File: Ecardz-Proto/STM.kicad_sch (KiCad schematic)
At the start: 0 parts

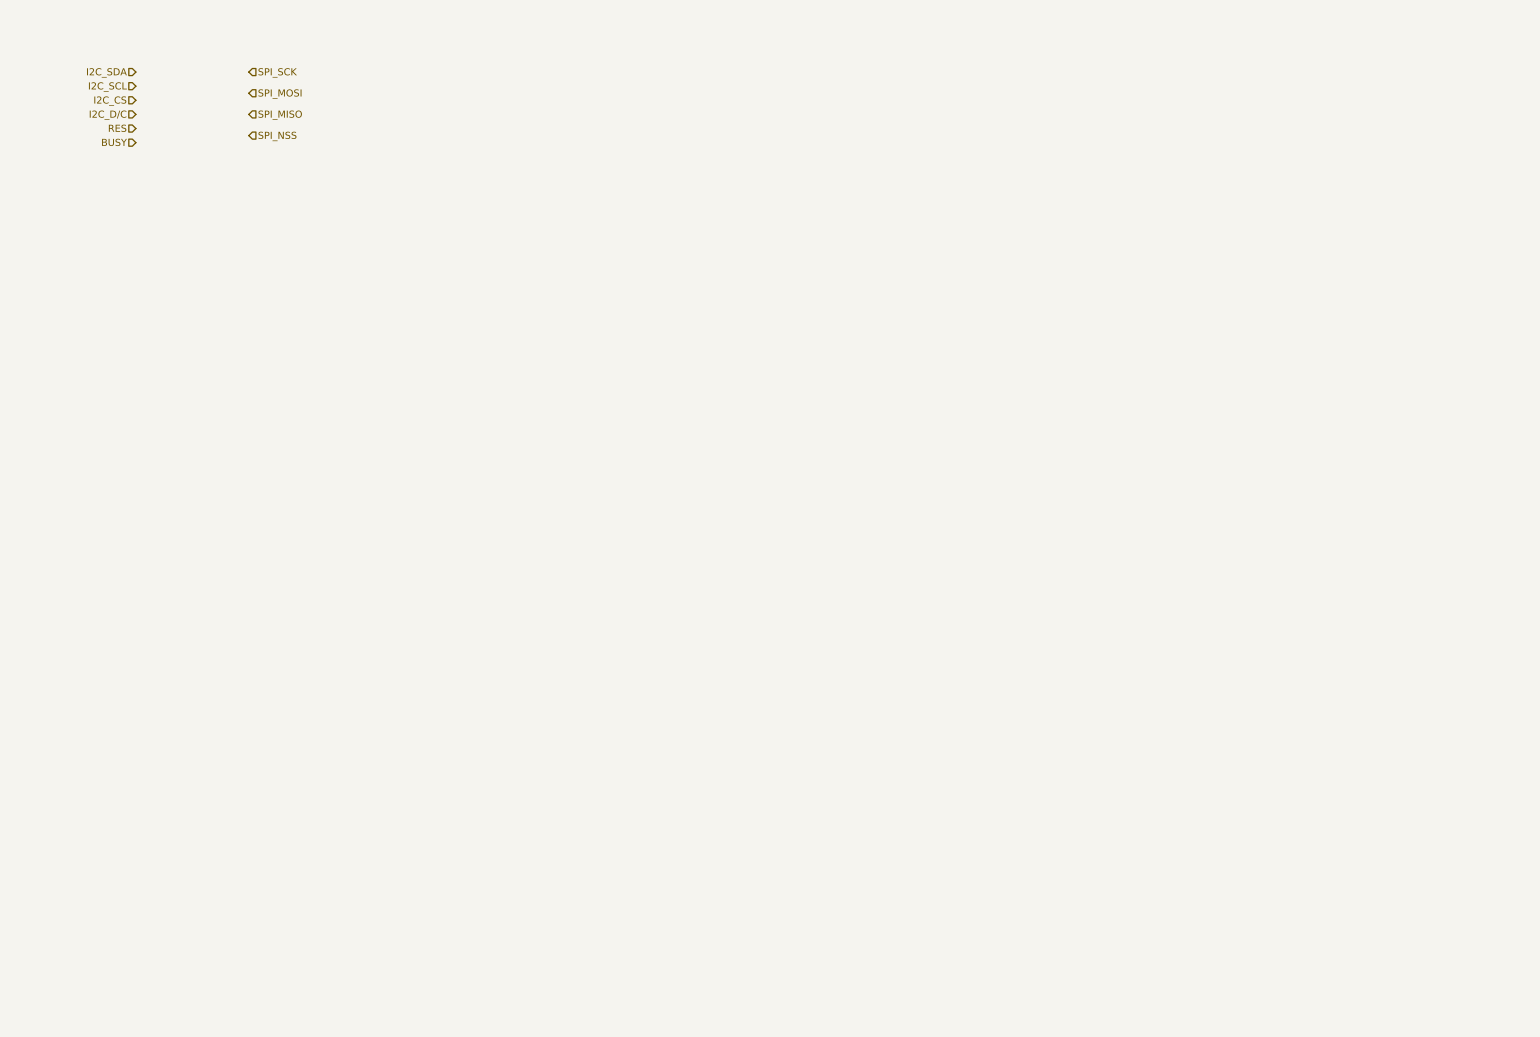
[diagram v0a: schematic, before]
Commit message: added STM and rpi pin connections.
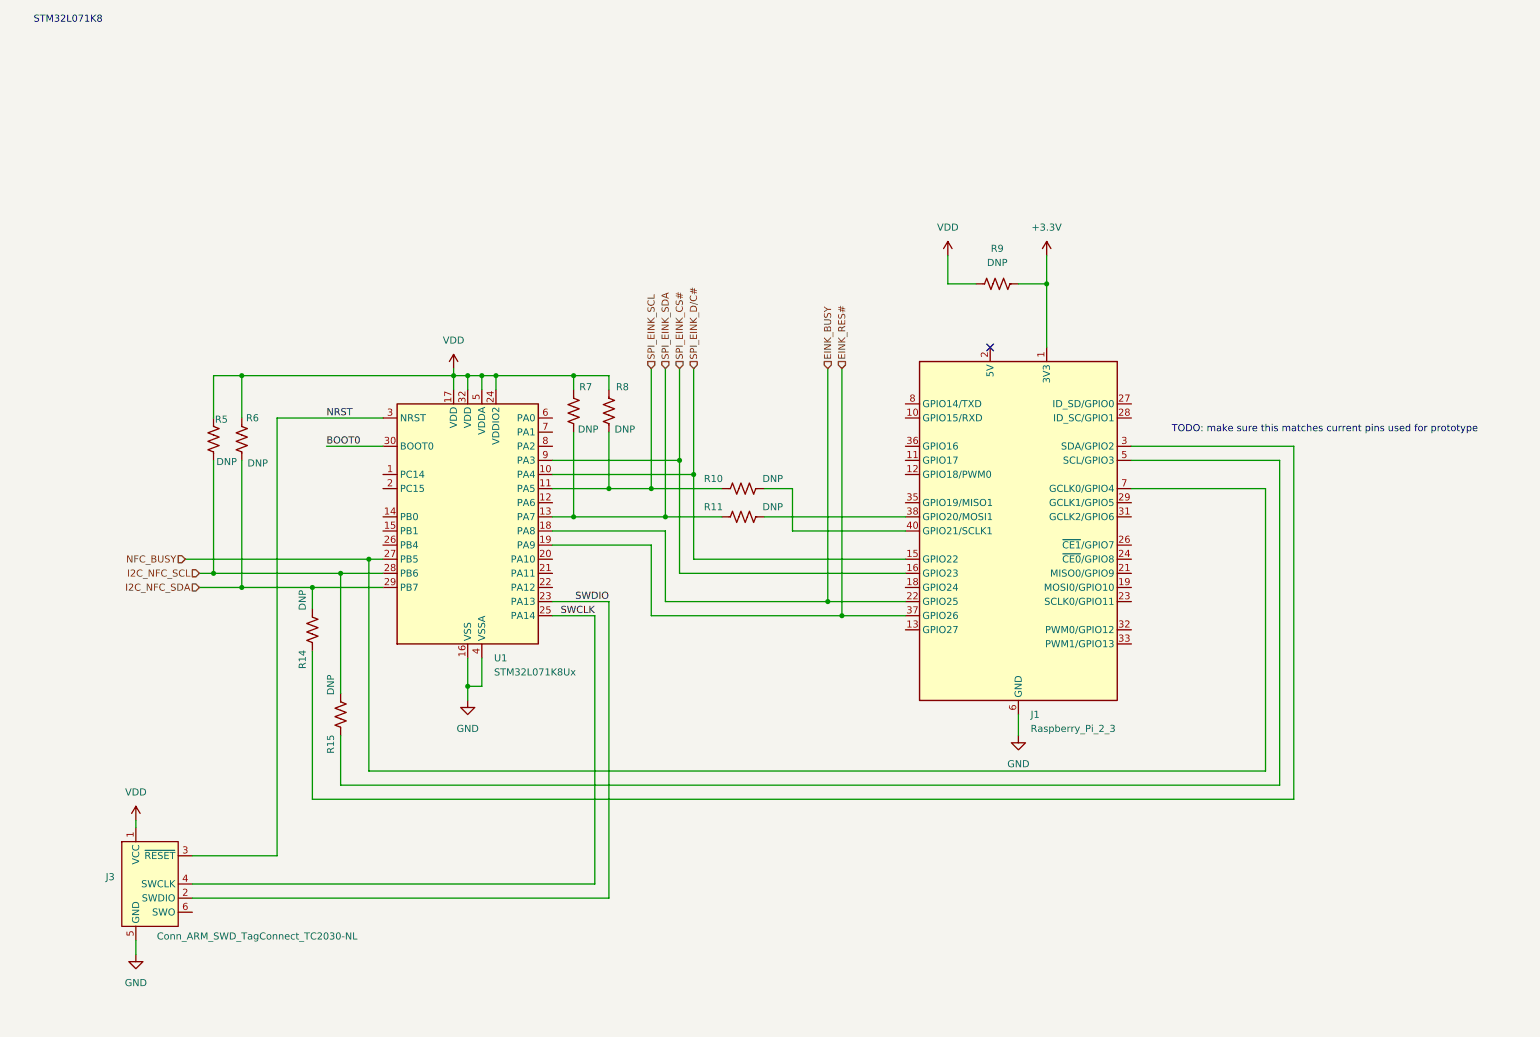
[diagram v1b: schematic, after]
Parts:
- added J1: Raspberry_Pi_2_3, symbol Connector:Raspberry_Pi_2_3
- added J3: Conn_ARM_SWD_TagConnect_TC2030-NL, Connector:Tag-Connect_TC2030-IDC-NL_2x03_P1.27mm_Vertical, symbol Connector:Conn_ARM_SWD_TagConnect_TC2030-NL
- added R10, R11, R14, R15, R5, R6, R7, R8, R9: DNP, Resistor_SMD:R_0603_1608Metric_Pad0.98x0.95mm_HandSolder, symbol Device:R_US
- added U1: STM32L071K8Ux, Package_DFN_QFN:QFN-32-1EP_5x5mm_P0.5mm_EP3.45x3.45mm, symbol MCU_ST_STM32L0:STM32L071K8Ux
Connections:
- new net: J1.5 (SCL/GPIO3), R15.1
- new net: J1.38 (GPIO20/MOSI1), R11.2
- new net: J1.2 (5V), J1.4 (5V)
- new net: J1.3 (SDA/GPIO2), R14.1
- new net: J1.40 (GPIO21/SCLK1), R10.2
- new net +3.3V: J1.1 (3V3), J1.17 (3V3), R9.2
- new net BOOT0: U1.30 (BOOT0)
- new net EINK_BUSY: J1.22 (GPIO25), U1.18 (PA8)
- new net EINK_RES#: J1.37 (GPIO26), U1.19 (PA9)
- new net GND: J1.14 (GND), J1.20 (GND), J1.25 (GND), J1.30 (GND), J1.34 (GND), J1.39 (GND), J1.6 (GND), J1.9 (GND), J3.5 (GND), U1.16 (VSS), U1.31 (VSS), U1.33 (VSS), U1.4 (VSSA)
- new net I2C_NFC_SCL: R15.2, R5.2, U1.28 (PB6)
- new net I2C_NFC_SDA: R14.2, R6.2, U1.29 (PB7)
- new net NFC_BUSY: J1.7 (GCLK0/GPIO4), U1.27 (PB5)
- new net NRST: J3.3 (~{RESET}), U1.3 (NRST)
- new net SPI_EINK_CS#: J1.16 (GPIO23), U1.9 (PA3)
- new net SPI_EINK_D/C#: J1.15 (GPIO22), U1.10 (PA4)
- new net SPI_EINK_SCL: R10.1, R8.2, U1.11 (PA5)
- new net SPI_EINK_SDA: R11.1, R7.2, U1.13 (PA7)
- new net SWCLK: J3.4 (SWCLK), U1.25 (PA14)
- new net SWDIO: J3.2 (SWDIO), U1.23 (PA13)
- new net VDD: J3.1 (VCC), R5.1, R6.1, R7.1, R8.1, R9.1, U1.17 (VDD), U1.24 (VDDIO2), U1.32 (VDD), U1.5 (VDDA)
- no-connect marks 0 -> 1
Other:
- note added: "STM32L071K8"
- note added: "TODO: make sure this matches current pins used for prototype"

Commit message: updated STM pinout
Updated RPI to just be breakout headers
Added JTAG connector and LPUSART
Updated to final? STM pinout
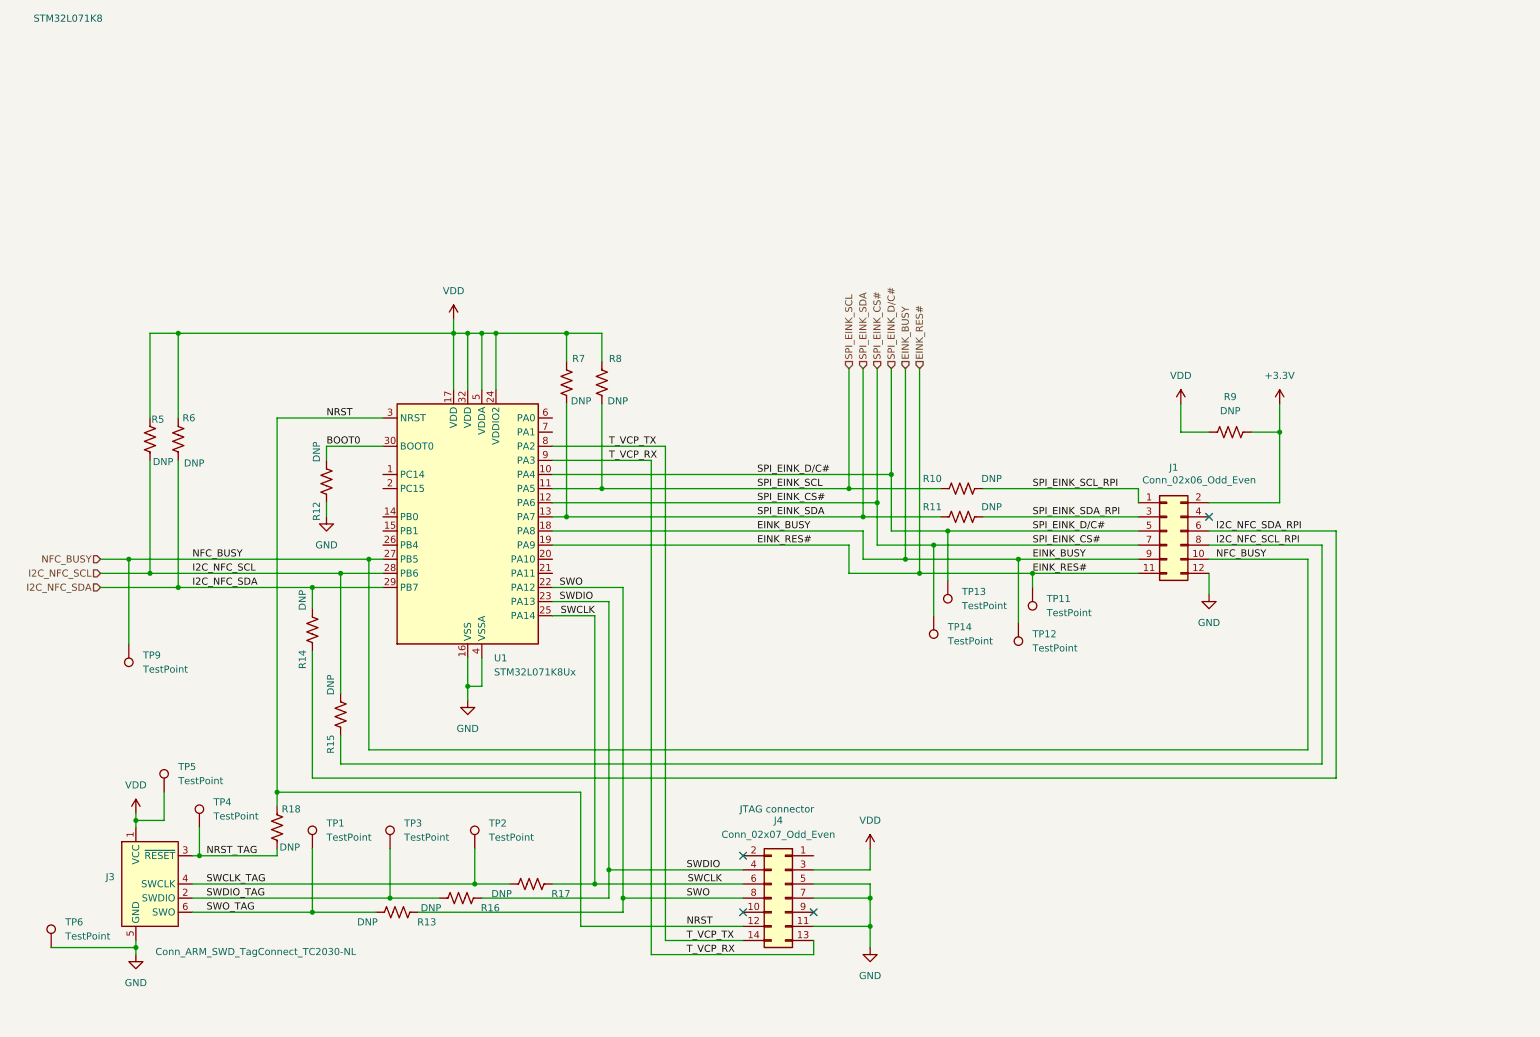
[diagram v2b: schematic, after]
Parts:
- removed J1: Raspberry_Pi_2_3, symbol Connector:Raspberry_Pi_2_3
- added J1: Conn_02x06_Odd_Even, symbol Connector_Generic:Conn_02x06_Odd_Even
- added J4: Conn_02x07_Odd_Even, symbol Connector_Generic:Conn_02x07_Odd_Even
- added R12, R13, R16, R17, R18: DNP, Resistor_SMD:R_0603_1608Metric_Pad0.98x0.95mm_HandSolder, symbol Device:R_US
- added TP1, TP11, TP12, TP13, TP14, TP2, TP3, TP4, TP5, TP6, TP9: TestPoint, symbol Connector:TestPoint
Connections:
- net +3.3V: now also J1.2 (Pin_2)
- net BOOT0: now also R12.2
- net EINK_BUSY: now also J1.9 (Pin_9), TP12.1
- net EINK_RES#: now also J1.11 (Pin_11), TP11.1
- net GND: now also J1.12 (Pin_12), J4.11 (Pin_11), J4.5 (Pin_5), J4.7 (Pin_7), R12.1, TP6.1
- net NFC_BUSY: now also J1.10 (Pin_10), TP9.1
- net NRST: now also J4.12 (Pin_12), R18.2; no longer J3.3 (~{RESET})
- net SPI_EINK_CS#: now also U1.12 (PA6), J1.7 (Pin_7), TP14.1; no longer U1.9 (PA3)
- net SPI_EINK_D/C#: now also J1.5 (Pin_5), TP13.1
- net SWCLK: now also J4.6 (Pin_6), R17.1; no longer J3.4 (SWCLK)
- net SWDIO: now also J4.4 (Pin_4), R16.1; no longer J3.2 (SWDIO)
- net VDD: now also J4.3 (Pin_3), TP5.1
- net I2C_NFC_SCL_RPI: now reaches R15.1
- net I2C_NFC_SCL_RPI: now also J1.8 (Pin_8)
- net SPI_EINK_SDA_RPI: now reaches R11.2
- net SPI_EINK_SDA_RPI: now also J1.3 (Pin_3)
- net I2C_NFC_SDA_RPI: now reaches R14.1
- net I2C_NFC_SDA_RPI: now also J1.6 (Pin_6)
- net SPI_EINK_SCL_RPI: now reaches R10.2
- net SPI_EINK_SCL_RPI: now also J1.1 (Pin_1)
- net SWO_TAG: now reaches J3.6 (SWO)
- net SWO_TAG: now also R13.2, TP1.1
- net SWO: now reaches U1.22 (PA12)
- net SWO: now also J4.8 (Pin_8), R13.1
- net T_VCP_TX: now reaches U1.8 (PA2)
- net T_VCP_TX: now also J4.14 (Pin_14)
- new net NRST_TAG: J3.3 (~{RESET}), R18.1, TP4.1
- new net SWCLK_TAG: J3.4 (SWCLK), R17.2, TP2.1
- new net SWDIO_TAG: J3.2 (SWDIO), R16.2, TP3.1
- new net T_VCP_RX: J4.13 (Pin_13), U1.9 (PA3)
- no-connect marks 1 -> 4
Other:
- note added: "JTAG connector"
- note removed: "TODO: make sure this matches current pins used for prototype"
- moved on the sheet: R10, R11, R5, R6, R7, R8, R9

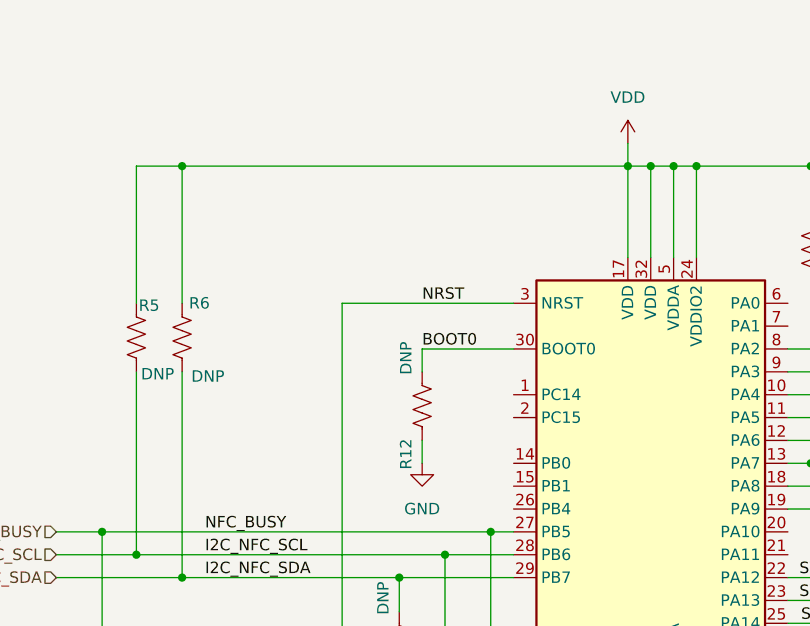
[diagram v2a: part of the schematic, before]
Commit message: added VDD cap
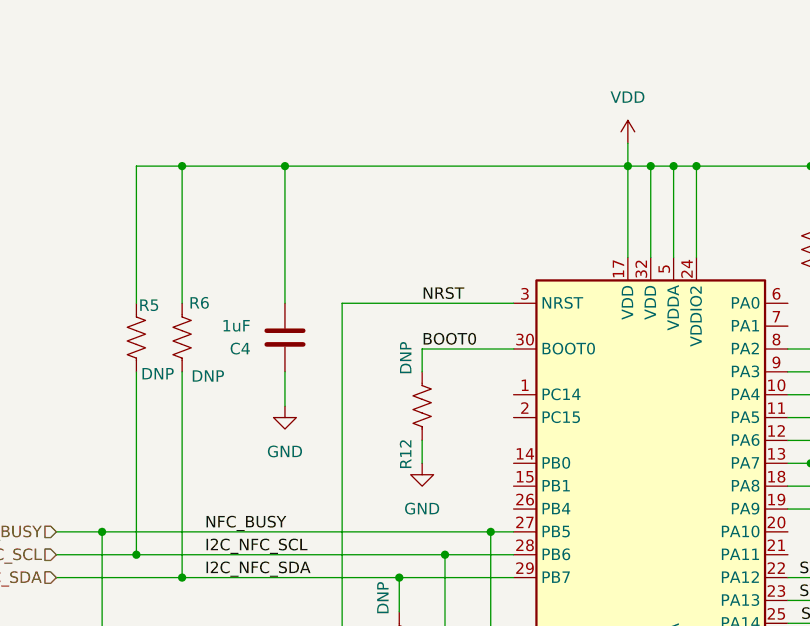
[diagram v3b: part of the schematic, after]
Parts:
- added C4: 1uF, Capacitor_SMD:C_0603_1608Metric_Pad1.08x0.95mm_HandSolder, symbol Device:C
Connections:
- net GND: now also C4.1
- net VDD: now also C4.2
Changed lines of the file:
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@@
 	)
 	(junction
+		(at 52.07 73.66)
+		(diameter 0)
+		(color 0 0 0 0)
+	)
+	(junction
 		(at 194.31 116.84)
 		(diameter 0)
@@
 	(wire
 		(pts
-			(xy 40.64 73.66) (xy 90.17 73.66)
+			(xy 40.64 73.66) (xy 52.07 73.66)
 		)
 		(stroke
@@
 	(wire
 		(pts
+			(xy 52.07 100.33) (xy 52.07 96.52)
+		)
+		(stroke
+			(width 0)
+			(type default)
+		)
+	)
+	(wire
+		(pts
 			(xy 120.65 175.26) (xy 142.24 175.26)
 		)
@@
 	(wire
 		(pts
+			(xy 52.07 73.66) (xy 90.17 73.66)
+		)
+		(stroke
+			(width 0)
+			(type default)
+		)
+	)
+	(wire
+		(pts
 			(xy 163.83 109.22) (xy 163.83 114.3)
 		)
@@
 	(wire
 		(pts
+			(xy 52.07 88.9) (xy 52.07 73.66)
+		)
+		(stroke
+			(width 0)
+			(type default)
+		)
+	)
+	(wire
+		(pts
 			(xy 67.31 96.52) (xy 67.31 93.98)
 		)
@@
 	(symbol
 		(lib_id "power:GND")
+		(at 52.07 100.33 0)
+		(unit 1)
+		(exclude_from_sim no)
+		(in_bom yes)
+		(on_board yes)
+		(dnp no)
+		(fields_autoplaced yes)
+		(property "Reference" "#PWR017"
+			(at 52.07 106.68 0)
+			(effects
+				(font
+					(size 1.27 1.27)
+				)
+				(hide yes)
+			)
+		)
+		(property "Value" "GND"
+			(at 52.07 105.41 0)
+			(effects
+				(font
+					(size 1.27 1.27)
+				)
+			)
+		)
+		(property "Footprint" ""
+			(at 52.07 100.33 0)
+			(effects
+				(font
+					(size 1.27 1.27)
+				)
+				(hide yes)
+			)
+		)
+		(property "Datasheet" ""
+			(at 52.07 100.33 0)
+			(effects
+				(font
+					(size 1.27 1.27)
+				)
+				(hide yes)
+			)
+		)
+		(property "Description" "Power symbol creates a global label with name \"GND\" , ground"
+			(at 52.07 100.33 0)
+			(effects
+				(font
+					(size 1.27 1.27)
+				)
+				(hide yes)
+			)
+		)
+		(pin "1"
+		)
+		(instances
+			(project "Ecardz-Proto"
+				(path "/2adbba85-9270-4efb-857d-656bb51406ca/fb28d19f-d7f8-44fd-bba1-2dc19a83839b"
+					(reference "#PWR017")
+					(unit 1)
+				)
+			)
+		)
+	)
+	(symbol
+		(lib_id "power:GND")
 		(at 165.1 184.15 0)
 		(mirror y)
@@
 					(unit 1)
 				)
+			)
+		)
+	)
+	(symbol
+		(lib_id "Device:C")
+		(at 52.07 92.71 180)
+		(unit 1)
+		(exclude_from_sim no)
+		(in_bom yes)
+		(on_board yes)
+		(dnp no)
+		(fields_autoplaced yes)
+		(property "Reference" "C4"
+			(at 48.26 93.9801 0)
+			(effects
+				(font
+					(size 1.27 1.27)
+				)
+				(justify left)
+			)
+		)
+		(property "Value" "1uF"
+			(at 48.26 91.4401 0)
+			(effects
+				(font
+					(size 1.27 1.27)
+				)
+				(justify left)
+			)
+		)
+		(property "Footprint" "Capacitor_SMD:C_0603_1608Metric_Pad1.08x0.95mm_HandSolder"
+			(at 51.1048 88.9 0)
+			(effects
+				(font
+					(size 1.27 1.27)
+				)
+				(hide yes)
+			)
+		)
+		(property "Datasheet" "https://www.yageo.com/upload/media/product/app/datasheet/mlcc/upy-gphc_x5r_4v-to-50v.pdf"
+			(at 52.07 92.71 0)
+			(effects
+				(font
+					(size 1.27 1.27)
+				)
+				(hide yes)
+			)
+		)
+		(property "Description" "Unpolarized capacitor"
+			(at 52.07 92.71 0)
+			(effects
+				(font
+					(size 1.27 1.27)
+				)
+				(hide yes)
+			)
+		)
+		(property "MANUFACTURER PART NUMBER" "CC0603KRX5R8BB105"
+			(at 52.07 92.71 0)
+			(effects
+				(font
+					(size 1.27 1.27)
+				)
+				(hide yes)
+			)
+		)
+		(property "Sim.Device" ""
+			(at 52.07 92.71 0)
+			(effects
+				(font
+					(size 1.27 1.27)
+				)
+				(hide yes)
+			)
+		)
+		(property "Sim.Pins" ""
+			(at 52.07 92.71 0)
+			(effects
+				(font
+					(size 1.27 1.27)
+				)
+				(hide yes)
+			)
+		)
+		(property "Sim.Type" ""
+			(at 52.07 92.71 0)
+			(effects
+				(font
+					(size 1.27 1.27)
+				)
+				(hide yes)
+			)
+		)
+		(pin "1"
+		)
+		(pin "2"
+		)
+		(instances
+			(project "Ecardz-Proto"
+				(path "/2adbba85-9270-4efb-857d-656bb51406ca/fb28d19f-d7f8-44fd-bba1-2dc19a83839b"
+					(reference "C4")
+					(unit 1)
+				)
